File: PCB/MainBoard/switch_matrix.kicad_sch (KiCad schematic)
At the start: 150 parts, among them SW10 SW_caps, SW11 SW_shift, SW12 SW_ctrl, SW13 SW_1, SW14 SW_q, SW15 SW_a, SW16 SW_z, SW17 SW_super, SW18 SW_2, SW19 SW_w, SW20 SW_s, SW21 SW_x, SW22 SW_alt, SW23 SW_3, SW24 SW_e, SW25 SW_4, SW26 SW_r, SW27 SW_f, SW28 SW_v, SW29 SW_c, SW30 SW_5, SW31 SW_t, SW32 SW_g, SW33 SW_b, SW34 SW_d, SW35 SW_6, SW36 SW_y, SW37 SW_h, SW38 SW_n, SW39 SW_space, SW4 SW_esc, SW40 SW_7, SW41 SW_u, SW42 SW_j, SW43 SW_m, SW44 SW_fn2, SW45 SW_8, SW46 SW_i, SW47 SW_k, SW48 SW_,, SW49 SW_left, SW5 SW_del, SW50 SW_9, SW51 SW_o, SW52 SW_l, SW53 SW_., SW54 SW_down, SW55 SW_0, SW56 SW_p, SW57 SW_;, SW58 SW_/, SW59 SW_up, SW6 SW_ins, SW60 SW_-, SW61 SW_[, SW62 SW_', SW63 SW_r_shift, SW64 SW_right, SW65 SW_+, SW66 SW_back, SW67 SW_], SW68 SW_\, SW69 SW_enter, SW7 SW_fn1, SW8 SW_`, SW9 SW_tab

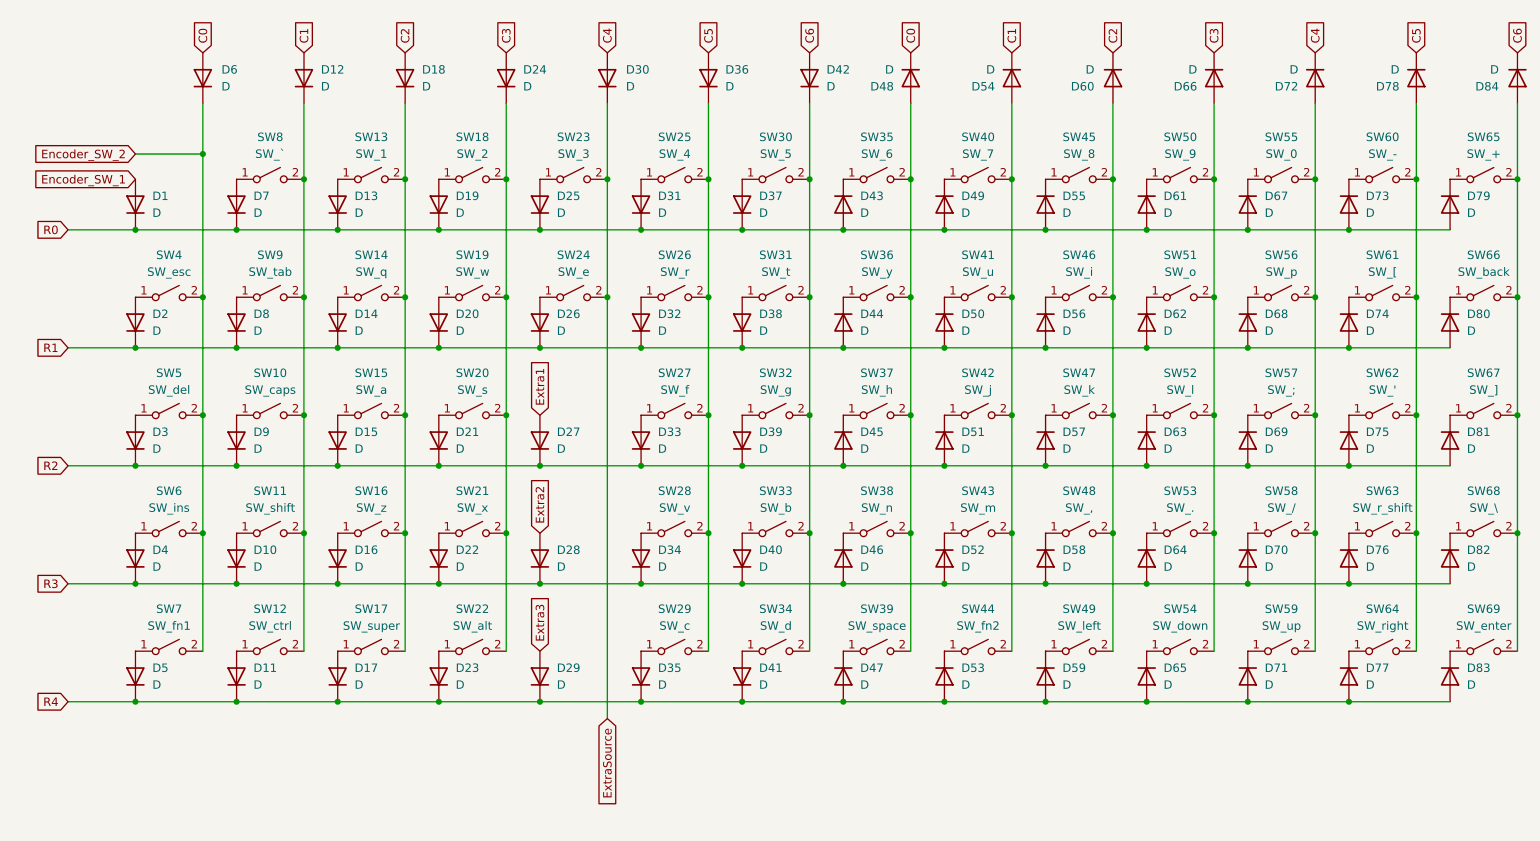
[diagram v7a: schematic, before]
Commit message: Added SMT pads to the diodes
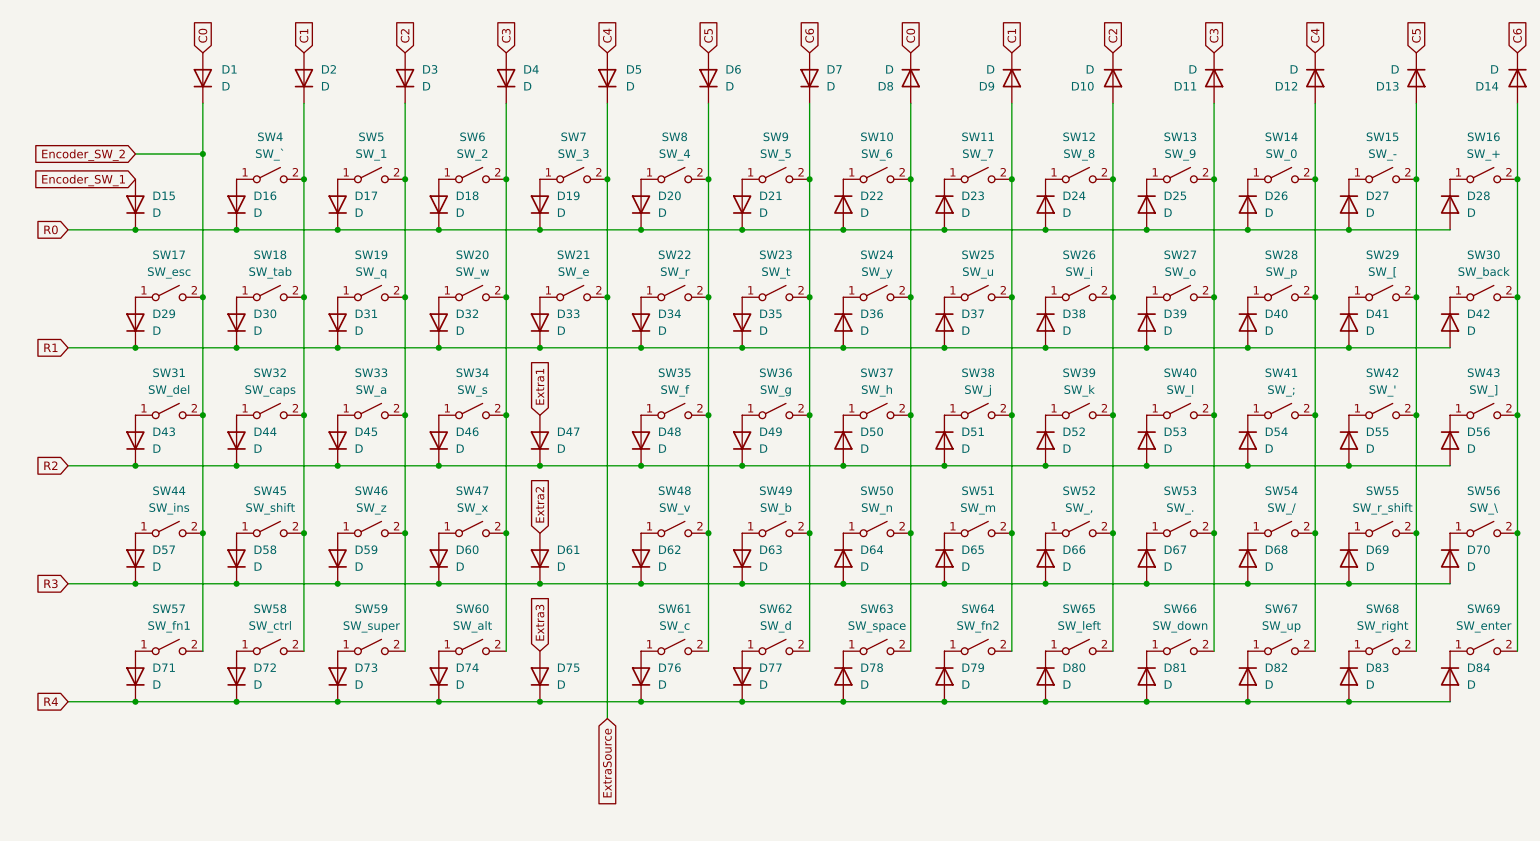
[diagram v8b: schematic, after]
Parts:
- renumbered D6 to D1, D60 to D10, D66 to D11, D72 to D12, D78 to D13, D84 to D14, D1 to D15, D7 to D16, D13 to D17, D19 to D18, D25 to D19, D12 to D2, D31 to D20, D37 to D21, D43 to D22, D49 to D23, D55 to D24, D61 to D25, D67 to D26, D73 to D27, D79 to D28, D2 to D29, D18 to D3, D8 to D30, D14 to D31, D20 to D32, D26 to D33, D32 to D34, D38 to D35, D44 to D36, D50 to D37, D56 to D38, D62 to D39, D24 to D4, D68 to D40, D74 to D41, D80 to D42, D3 to D43, D9 to D44, D15 to D45, D21 to D46, D27 to D47, D33 to D48, D39 to D49, D30 to D5, D45 to D50, D57 to D52, D63 to D53, D69 to D54, D75 to D55, D81 to D56, D4 to D57, D10 to D58, D16 to D59, D36 to D6, D22 to D60, D28 to D61, D34 to D62, D40 to D63, D46 to D64, D52 to D65, D58 to D66, D64 to D67, D70 to D68, D76 to D69, D42 to D7, D82 to D70, D5 to D71, D11 to D72, D17 to D73, D23 to D74, D29 to D75, D35 to D76, D41 to D77, D47 to D78, D53 to D79, D48 to D8, D59 to D80, D65 to D81, D71 to D82, D77 to D83, D83 to D84, D54 to D9, SW35 to SW10, SW40 to SW11, SW45 to SW12, SW50 to SW13, SW55 to SW14, SW60 to SW15, SW65 to SW16, SW4 to SW17, SW9 to SW18, SW14 to SW19, SW19 to SW20, SW24 to SW21, SW26 to SW22, SW31 to SW23, SW36 to SW24, SW41 to SW25, SW46 to SW26, SW51 to SW27, SW56 to SW28, SW61 to SW29, SW66 to SW30, SW5 to SW31, SW10 to SW32, SW15 to SW33, SW20 to SW34, SW27 to SW35, SW32 to SW36, SW42 to SW38, SW47 to SW39, SW8 to SW4, SW52 to SW40, SW57 to SW41, SW62 to SW42, SW67 to SW43, SW6 to SW44, SW11 to SW45, SW16 to SW46, SW21 to SW47, SW28 to SW48, SW33 to SW49, SW13 to SW5, SW38 to SW50, SW43 to SW51, SW48 to SW52, SW58 to SW54, SW63 to SW55, SW68 to SW56, SW7 to SW57, SW12 to SW58, SW17 to SW59, SW18 to SW6, SW22 to SW60, SW29 to SW61, SW34 to SW62, SW39 to SW63, SW44 to SW64, SW49 to SW65, SW54 to SW66, SW59 to SW67, SW64 to SW68, SW23 to SW7, SW25 to SW8, SW30 to SW9
